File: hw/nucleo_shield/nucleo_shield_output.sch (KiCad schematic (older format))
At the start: 8 parts, among them P10 CONN_OUTH1, P11 CONN_OUTH2, P2 CONN_OUT2, P3 CONN_OUT1, U1 74HC595, U10 ULN2803, U2 74HC595, U9 ULN2803

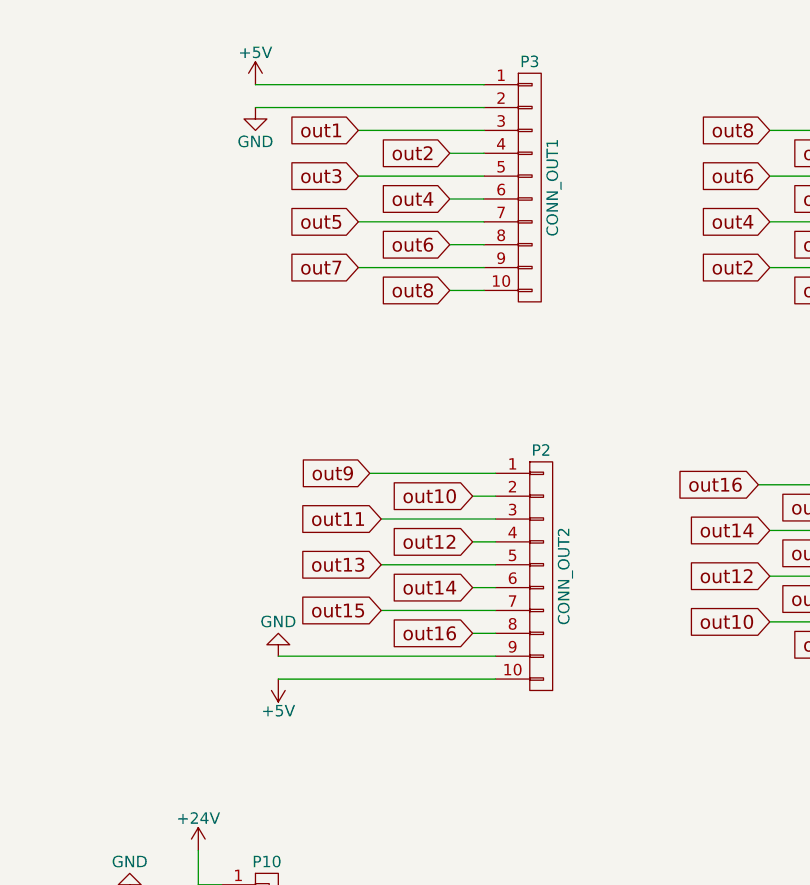
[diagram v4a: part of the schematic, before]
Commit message: Nucleo: Rework connection
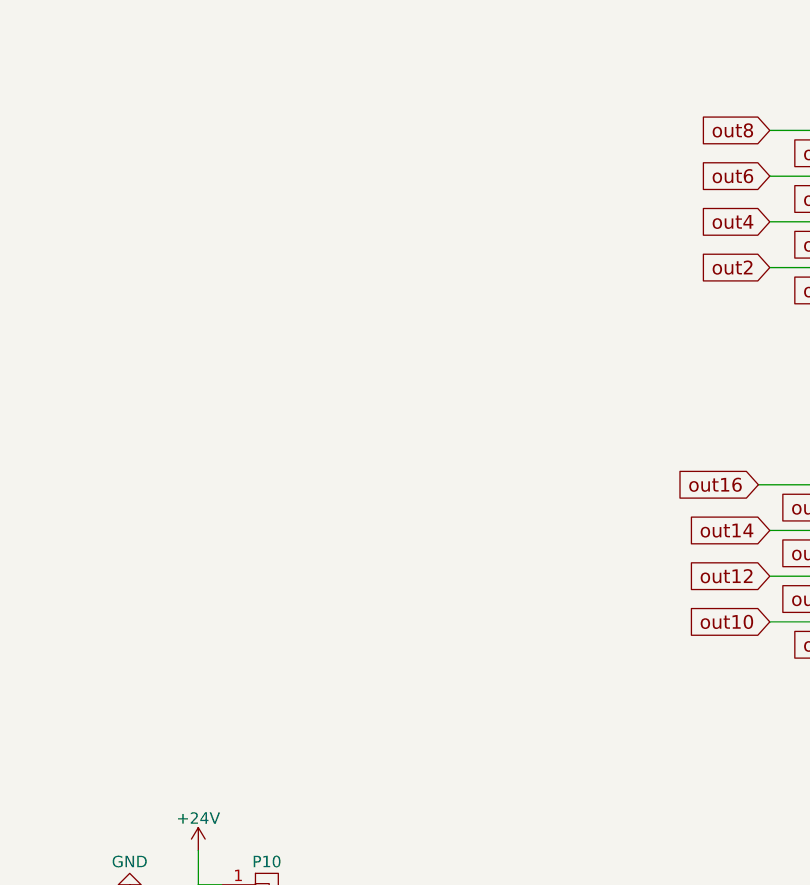
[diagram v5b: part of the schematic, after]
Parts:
- removed P2: CONN_OUT2, Pin_Headers:Pin_Header_Straight_1x10, symbol CONN_01X10
- removed P3: CONN_OUT1, Pin_Headers:Pin_Header_Straight_1x10, symbol CONN_01X10
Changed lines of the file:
@@
 LIBS:memory
 LIBS:xilinx
-LIBS:special
 LIBS:microcontrollers
 LIBS:dsp
@@
 Wire Wire Line
 	3750 1150 4100 1150
-Text GLabel 6500 1150 0    60   Input ~ 0
-out1
-Text GLabel 6900 1250 0    60   Input ~ 0
-out2
-Text GLabel 6500 1350 0    60   Input ~ 0
-out3
-Text GLabel 6900 1450 0    60   Input ~ 0
-out4
-Text GLabel 6500 1550 0    60   Input ~ 0
-out5
-Text GLabel 6900 1650 0    60   Input ~ 0
-out6
-Text GLabel 6500 1750 0    60   Input ~ 0
-out7
 Text GLabel 4400 3450 2    60   Input ~ 0
 out16
-Text GLabel 6900 1850 0    60   Input ~ 0
-out8
-Text GLabel 6550 2650 0    60   Input ~ 0
-out9
-Text GLabel 7000 2750 0    60   Input ~ 0
-out10
-Text GLabel 6600 2850 0    60   Input ~ 0
-out11
-Text GLabel 7000 2950 0    60   Input ~ 0
-out12
-Text GLabel 6600 3050 0    60   Input ~ 0
-out13
-Text GLabel 7000 3150 0    60   Input ~ 0
-out14
-Text GLabel 6600 3250 0    60   Input ~ 0
-out15
-Text GLabel 7000 3350 0    60   Input ~ 0
-out16
-Wire Wire Line
-	6500 1150 7050 1150
-Wire Wire Line
-	6900 1250 7050 1250
-Wire Wire Line
-	6500 1350 7050 1350
-Wire Wire Line
-	6900 1450 7050 1450
-Wire Wire Line
-	7050 1550 6500 1550
-Wire Wire Line
-	6900 1650 7050 1650
-Wire Wire Line
-	7050 1750 6500 1750
-Wire Wire Line
-	6900 1850 7050 1850
-Wire Wire Line
-	7000 2750 7100 2750
-Wire Wire Line
-	7100 2850 6600 2850
-Wire Wire Line
-	7000 2950 7100 2950
-Wire Wire Line
-	7100 3050 6600 3050
-Wire Wire Line
-	7000 3150 7100 3150
-Wire Wire Line
-	7100 3250 6600 3250
-Wire Wire Line
-	7000 3350 7100 3350
-$Comp
-L GND #PWR024
-U 1 1 5729ABA1
-P 6050 1050
-F 0 "#PWR024" H 6050 800 50  0001 C CNN
-F 1 "GND" H 6050 900 50  0000 C CNN
-F 2 "" H 6050 1050 60  0000 C CNN
-F 3 "" H 6050 1050 60  0000 C CNN
-	1    6050 1050
-	1    0    0    -1
-$EndComp
-Wire Wire Line
-	6550 2650 7100 2650
-$Comp
-L +5V #PWR025
-U 1 1 5729ABA8
-P 6050 950
-F 0 "#PWR025" H 6050 800 50  0001 C CNN
-F 1 "+5V" H 6050 1090 50  0000 C CNN
-F 2 "" H 6050 950 60  0000 C CNN
-F 3 "" H 6050 950 60  0000 C CNN
-	1    6050 950
-	1    0    0    -1
-$EndComp
-$Comp
-L CONN_01X10 P3
-U 1 1 5729ABAE
-P 7250 1400
-F 0 "P3" H 7250 1950 50  0000 C CNN
-F 1 "CONN_OUT1" V 7350 1400 50  0000 C CNN
-F 2 "Pin_Headers:Pin_Header_Straight_1x10" H 7250 1400 60  0001 C CNN
-F 3 "" H 7250 1400 60  0000 C CNN
-	1    7250 1400
-	1    0    0    -1
-$EndComp
-Wire Wire Line
-	6050 1050 7050 1050
-Wire Wire Line
-	7050 950  6050 950
-$Comp
-L CONN_01X10 P2
-U 1 1 5729ABB7
-P 7300 3100
-F 0 "P2" H 7300 3650 50  0000 C CNN
-F 1 "CONN_OUT2" V 7400 3100 50  0000 C CNN
-F 2 "Pin_Headers:Pin_Header_Straight_1x10" H 7300 3100 60  0001 C CNN
-F 3 "" H 7300 3100 60  0000 C CNN
-	1    7300 3100
-	1    0    0    -1
-$EndComp
-$Comp
-L +5V #PWR026
-U 1 1 5729ABBE
-P 6150 3550
-F 0 "#PWR026" H 6150 3400 50  0001 C CNN
-F 1 "+5V" H 6150 3690 50  0000 C CNN
-F 2 "" H 6150 3550 60  0000 C CNN
-F 3 "" H 6150 3550 60  0000 C CNN
-	1    6150 3550
-	-1   0    0    1
-$EndComp
-$Comp
-L GND #PWR027
-U 1 1 5729ABC4
-P 6150 3450
-F 0 "#PWR027" H 6150 3200 50  0001 C CNN
-F 1 "GND" H 6150 3300 50  0000 C CNN
-F 2 "" H 6150 3450 60  0000 C CNN
-F 3 "" H 6150 3450 60  0000 C CNN
-	1    6150 3450
-	-1   0    0    1
-$EndComp
-Wire Wire Line
-	7100 3450 6150 3450
-Wire Wire Line
-	6150 3550 7100 3550
 Wire Wire Line
 	2350 1450 1050 1450
@@
 $EndComp
 $Comp
-L +5V #PWR028
+L +5V #PWR024
 U 1 1 5729ABD5
 P 2750 850
-F 0 "#PWR028" H 2750 700 50  0001 C CNN
+F 0 "#PWR024" H 2750 700 50  0001 C CNN
 F 1 "+5V" H 2750 990 50  0000 C CNN
 F 2 "" H 2750 850 60  0000 C CNN
@@
 $EndComp
 $Comp
-L +5V #PWR029
+L +5V #PWR025
 U 1 1 5729ABDB
 P 4450 2500
-F 0 "#PWR029" H 4450 2350 50  0001 C CNN
+F 0 "#PWR025" H 4450 2350 50  0001 C CNN
 F 1 "+5V" H 4450 2640 50  0000 C CNN
 F 2 "" H 4450 2500 60  0000 C CNN
@@
 	3750 2300 3750 2050
 $Comp
-L +5V #PWR030
+L +5V #PWR026
 U 1 1 5729ABE8
 P 1050 1450
-F 0 "#PWR030" H 1050 1300 50  0001 C CNN
+F 0 "#PWR026" H 1050 1300 50  0001 C CNN
 F 1 "+5V" H 1050 1590 50  0000 C CNN
 F 2 "" H 1050 1450 60  0000 C CNN
@@
 $EndComp
 $Comp
-L +5V #PWR031
+L +5V #PWR027
 U 1 1 5729ABEE
 P 1600 3050
-F 0 "#PWR031" H 1600 2900 50  0001 C CNN
+F 0 "#PWR027" H 1600 2900 50  0001 C CNN
 F 1 "+5V" H 1600 3190 50  0000 C CNN
 F 2 "" H 1600 3050 60  0000 C CNN
@@
 $EndComp
 $Comp
-L GND #PWR032
+L GND #PWR028
 U 1 1 57307D6B
 P 9250 2000
-F 0 "#PWR032" H 9250 1750 50  0001 C CNN
+F 0 "#PWR028" H 9250 1750 50  0001 C CNN
 F 1 "GND" H 9250 1850 50  0000 C CNN
 F 2 "" H 9250 2000 60  0000 C CNN
@@
 $EndComp
 $Comp
-L GND #PWR033
+L GND #PWR029
 U 1 1 57307D82
 P 9200 3550
-F 0 "#PWR033" H 9200 3300 50  0001 C CNN
+F 0 "#PWR029" H 9200 3300 50  0001 C CNN
 F 1 "GND" H 9200 3400 50  0000 C CNN
 F 2 "" H 9200 3550 60  0000 C CNN
@@
 $EndComp
 $Comp
-L +24V #PWR034
+L +24V #PWR030
 U 1 1 57307DA1
 P 9250 1000
-F 0 "#PWR034" H 9250 850 50  0001 C CNN
+F 0 "#PWR030" H 9250 850 50  0001 C CNN
 F 1 "+24V" H 9250 1140 50  0000 C CNN
 F 2 "" H 9250 1000 60  0000 C CNN
@@
 $EndComp
 $Comp
-L +24V #PWR035
+L +24V #PWR031
 U 1 1 57307DBF
 P 9200 2550
-F 0 "#PWR035" H 9200 2400 50  0001 C CNN
+F 0 "#PWR031" H 9200 2400 50  0001 C CNN
 F 1 "+24V" H 9200 2690 50  0000 C CNN
 F 2 "" H 9200 2550 60  0000 C CNN
@@
 	5750 5350 5900 5350
 $Comp
-L GND #PWR036
+L GND #PWR032
 U 1 1 573085F0
 P 5500 4500
-F 0 "#PWR036" H 5500 4250 50  0001 C CNN
+F 0 "#PWR032" H 5500 4250 50  0001 C CNN
 F 1 "GND" H 5500 4350 50  0000 C CNN
 F 2 "" H 5500 4500 60  0000 C CNN
@@
 $EndComp
 $Comp
-L GND #PWR037
+L GND #PWR033
 U 1 1 5730860B
 P 4800 6800
-F 0 "#PWR037" H 4800 6550 50  0001 C CNN
+F 0 "#PWR033" H 4800 6550 50  0001 C CNN
 F 1 "GND" H 4800 6650 50  0000 C CNN
 F 2 "" H 4800 6800 60  0000 C CNN
@@
 	5900 6800 4800 6800
 $Comp
-L +24V #PWR038
+L +24V #PWR034
 U 1 1 573087B8
 P 5800 4300
-F 0 "#PWR038" H 5800 4150 50  0001 C CNN
+F 0 "#PWR034" H 5800 4150 50  0001 C CNN
 F 1 "+24V" H 5800 4440 50  0000 C CNN
 F 2 "" H 5800 4300 60  0000 C CNN
@@
 	5800 4450 5900 4450
 $Comp
-L +24V #PWR039
+L +24V #PWR035
 U 1 1 5730884E
 P 4500 6900
-F 0 "#PWR039" H 4500 6750 50  0001 C CNN
+F 0 "#PWR035" H 4500 6750 50  0001 C CNN
 F 1 "+24V" H 4500 7040 50  0000 C CNN
 F 2 "" H 4500 6900 60  0000 C CNN

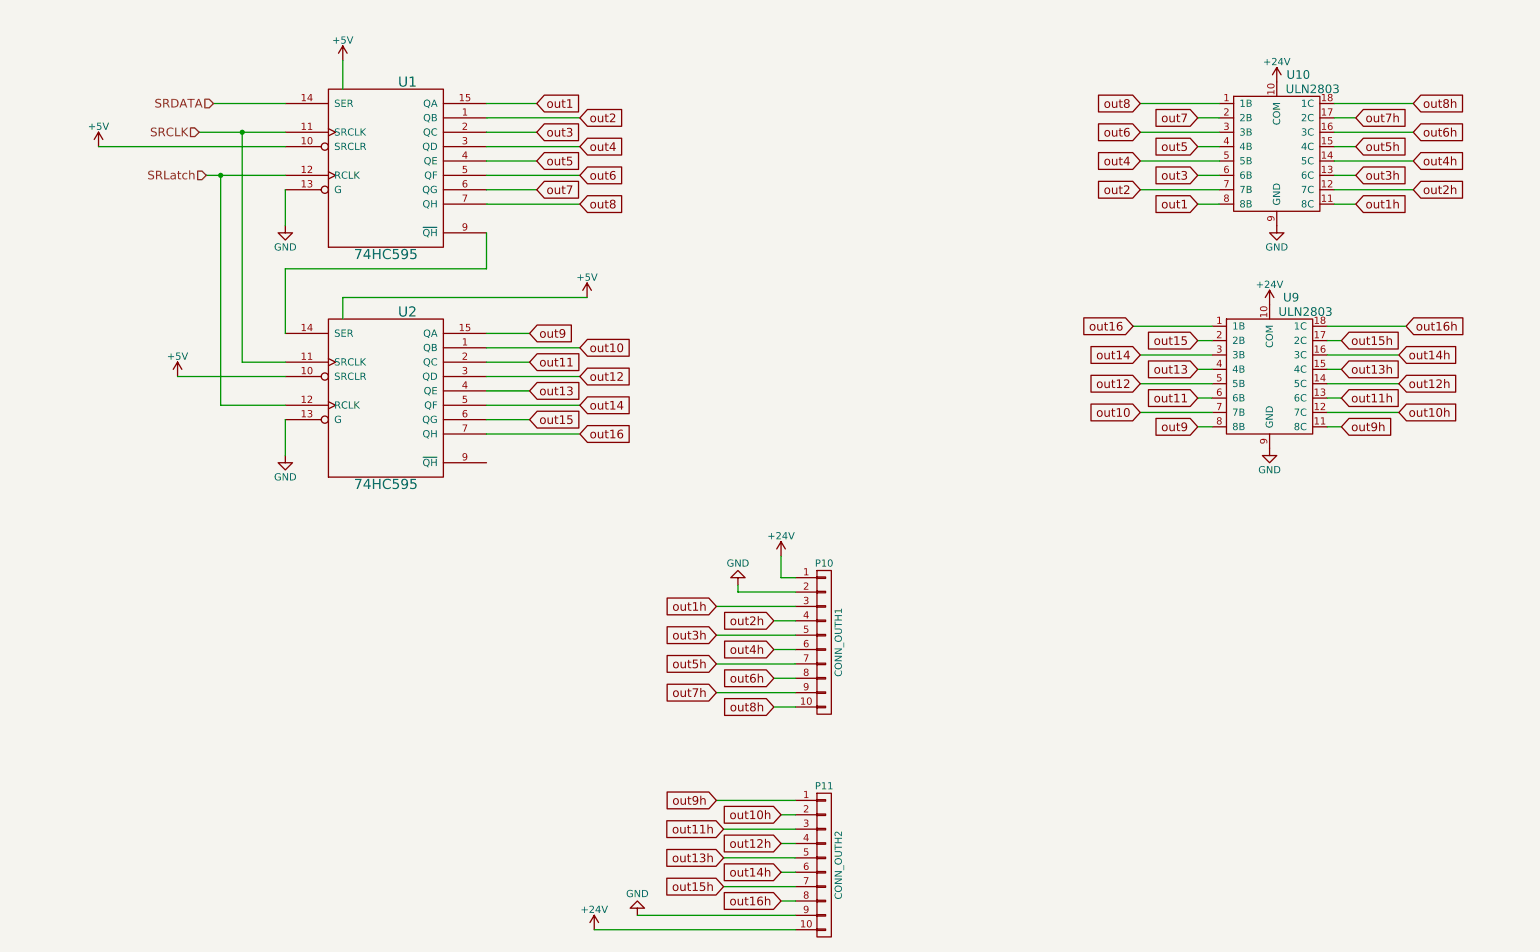
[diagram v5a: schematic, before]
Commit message: Add one more shift register
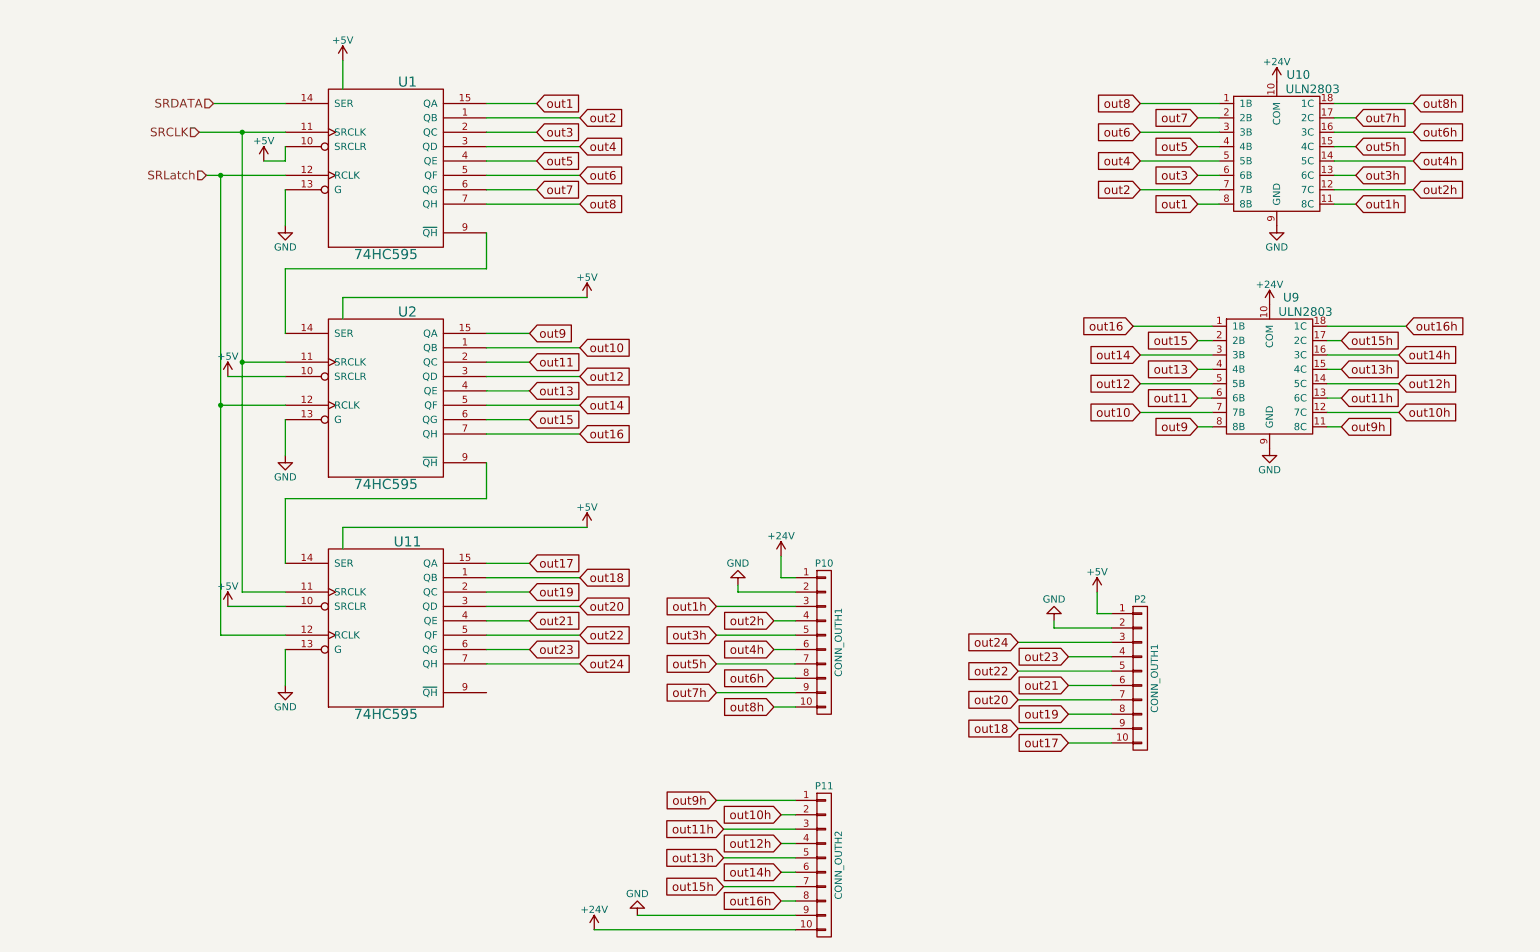
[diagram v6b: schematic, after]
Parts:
- added P2: CONN_OUTH1, w_conn_screw:mors_10p, symbol CONN_01X10
- added U11: 74HC595, Housings_DIP:DIP-16_W7.62mm, symbol 74HC595
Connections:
- net +5V: now also P2.1 (P1), U11.10 (SRCLR), U11.16 (VCC)
- net GND: now also P2.2 (P2), U11.13 (G), U11.8 (GND)
- net SRCLK: now also U11.11 (SRCLK)
- net SRLatch: now also U11.12 (RCLK)
- net at U2.9 (~QH): now also U11.14 (SER)
- new net out17: P2.10 (P10), U11.15 (QA)
- new net out18: P2.9 (P9), U11.1 (QB)
- new net out19: P2.8 (P8), U11.2 (QC)
- new net out20: P2.7 (P7), U11.3 (QD)
- new net out21: P2.6 (P6), U11.4 (QE)
- new net out22: P2.5 (P5), U11.5 (QF)
- new net out23: P2.4 (P4), U11.6 (QG)
- new net out24: P2.3 (P3), U11.7 (QH)

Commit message: Nucleo: add jumpers and outputs
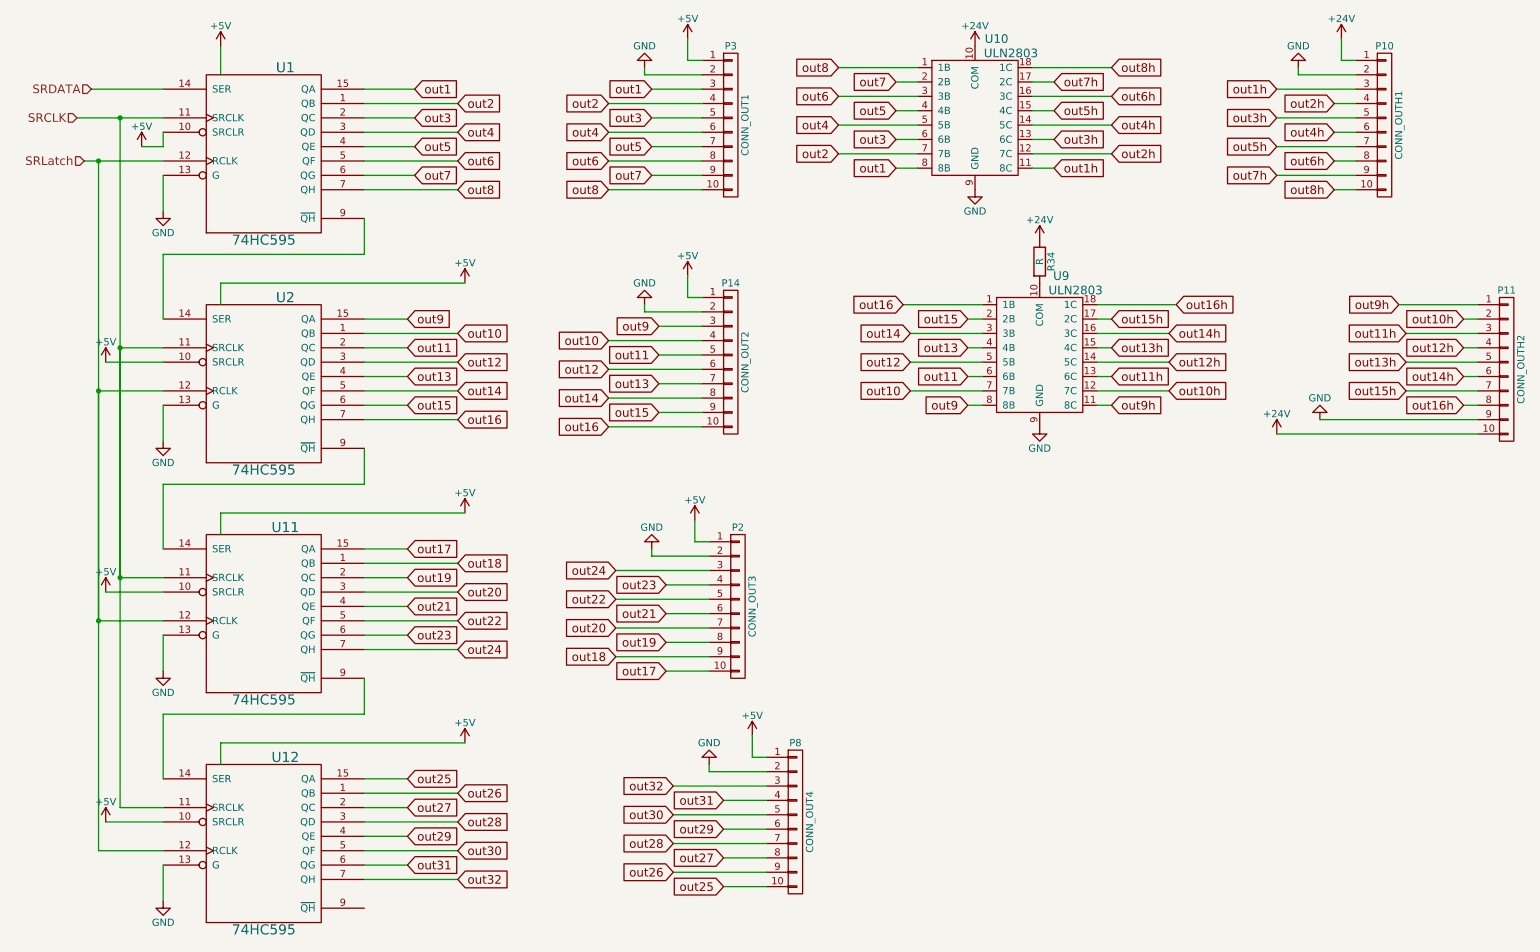
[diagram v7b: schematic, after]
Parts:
- added P14: CONN_OUT2, Pin_Headers:Pin_Header_Straight_1x10, symbol CONN_01X10
- added P3: CONN_OUT1, Pin_Headers:Pin_Header_Straight_1x10, symbol CONN_01X10
- added P8: CONN_OUT4, Pin_Headers:Pin_Header_Straight_1x10, symbol CONN_01X10
- added R34: R, Resistors_ThroughHole:Resistor_Horizontal_RM10mm, symbol R
- added U12: 74HC595, Housings_DIP:DIP-16__300, symbol 74HC595
- P2: value CONN_OUTH1 -> CONN_OUT3; footprint w_conn_screw:mors_10p -> Pin_Headers:Pin_Header_Straight_1x10
- U11: footprint Housings_DIP:DIP-16_W7.62mm -> Housings_DIP:DIP-16__300
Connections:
- net +24V: now also R34.1; no longer U9.10 (COM)
- net +5V: now also P14.1 (P1), P3.1 (P1), P8.1 (P1), U12.10 (SRCLR), U12.16 (VCC)
- net GND: now also P14.2 (P2), P3.2 (P2), P8.2 (P2), U12.13 (G), U12.8 (GND)
- net SRCLK: now also U12.11 (SRCLK)
- net SRLatch: now also U12.12 (RCLK)
- net out1: now also P3.3 (P3)
- net out10: now also P14.4 (P4)
- net out11: now also P14.5 (P5)
- net out12: now also P14.6 (P6)
- net out13: now also P14.7 (P7)
- net out14: now also P14.8 (P8)
- net out15: now also P14.9 (P9)
- net out16: now also P14.10 (P10)
- net out2: now also P3.4 (P4)
- net out3: now also P3.5 (P5)
- net out4: now also P3.6 (P6)
- net out5: now also P3.7 (P7)
- net out6: now also P3.8 (P8)
- net out7: now also P3.9 (P9)
- net out8: now also P3.10 (P10)
- net out9: now also P14.3 (P3)
- net at U11.9 (~QH): now also U12.14 (SER)
- new net: R34.2, U9.10 (COM)
- new net out25: P8.10 (P10), U12.15 (QA)
- new net out26: P8.9 (P9), U12.1 (QB)
- new net out27: P8.8 (P8), U12.2 (QC)
- new net out28: P8.7 (P7), U12.3 (QD)
- new net out29: P8.6 (P6), U12.4 (QE)
- new net out30: P8.5 (P5), U12.5 (QF)
- new net out31: P8.4 (P4), U12.6 (QG)
- new net out32: P8.3 (P3), U12.7 (QH)
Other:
- moved on the sheet: P10, P11, P2, U1, U10, U11, U2, U9
